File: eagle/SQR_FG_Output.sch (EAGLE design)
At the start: 17 parts, among them IC2 NJM7032, T1 2SK4017, T2 2SK4017

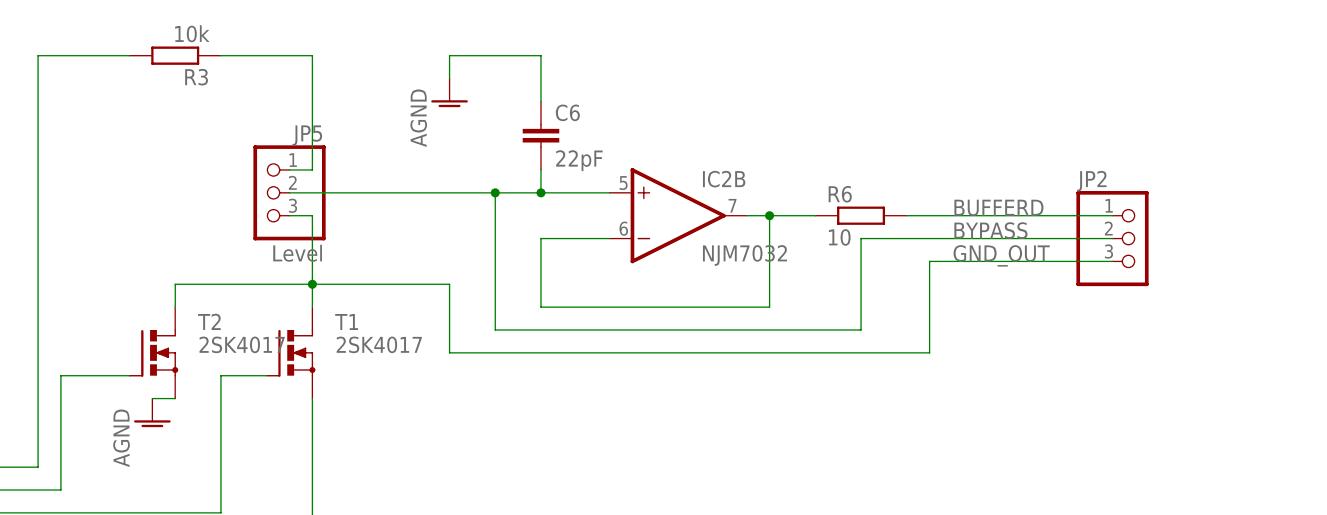
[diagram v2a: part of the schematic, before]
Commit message: SQR_FG_Output.sch LC 2次LPFを追加
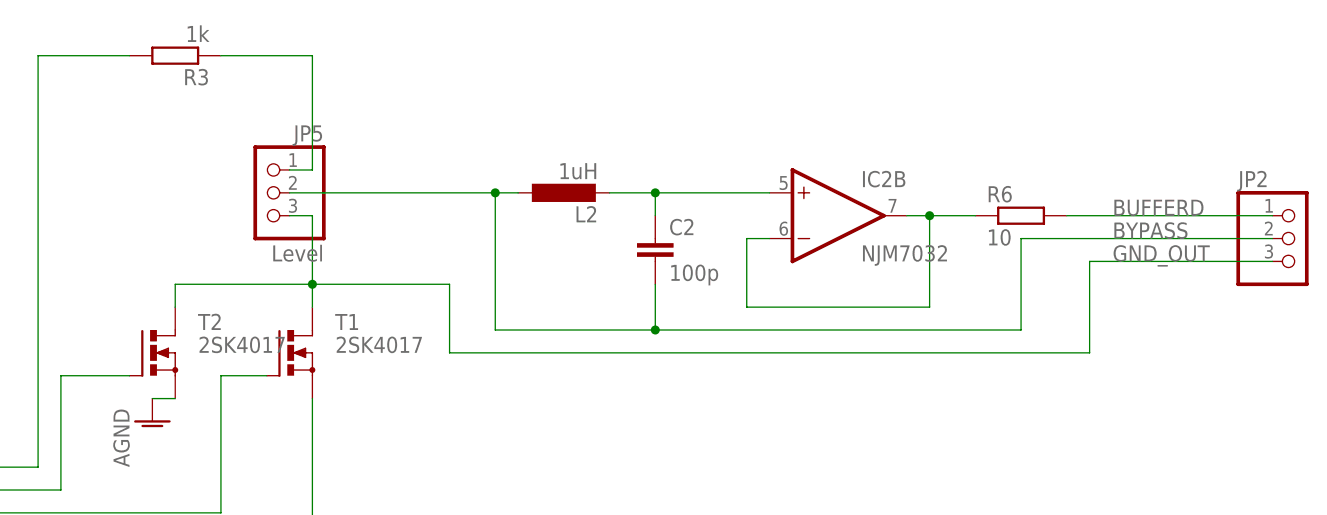
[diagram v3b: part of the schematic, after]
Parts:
- removed C6: 22pF, rcl:C-EU025-024X044
- added C2: 100p, rcl:C-EU050-024X044
- added L2: 1uH, rcl:L-EU0204/7
- R3: value 10k -> 1k
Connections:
- new net N$1: C2.1, IC2B.+IN, L2.2
- net AGND: no longer C6.1
- net BYPASS: now also C2.2, L2.1; no longer C6.2, IC2B.+IN
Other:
- moved on the sheet: IC2B, JP2, R6
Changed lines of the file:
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@@
 <setting verticaltext="up"/>
 </settings>
-<grid distance="0.1" unitdist="inch" unit="inch" style="dots" multiple="1" display="yes" altdistance="0.01" altunitdist="inch" altunit="inch"/>
+<grid distance="0.1" unitdist="inch" unit="inch" style="lines" multiple="1" display="no" altdistance="0.01" altunitdist="inch" altunit="inch"/>
 <layers>
 <layer number="1" name="Top" color="4" fill="1" visible="no" active="no"/>
@@
 <part name="T2" library="transistor-power" deviceset="RD06HVF1" device="" value="2SK4017"/>
 <part name="C5" library="rcl" deviceset="C-EU" device="025-024X044" value="0.1uF"/>
-<part name="R3" library="rcl" deviceset="R-EU_" device="0207/7" value="10k"/>
-<part name="C6" library="rcl" deviceset="C-EU" device="025-024X044" value="22pF"/>
+<part name="R3" library="rcl" deviceset="R-EU_" device="0207/7" value="1k"/>
 <part name="AGND1" library="supply1" deviceset="AGND" device=""/>
-<part name="AGND2" library="supply1" deviceset="AGND" device=""/>
 <part name="AGND3" library="supply1" deviceset="AGND" device=""/>
 <part name="AGND5" library="supply1" deviceset="AGND" device=""/>
@@
 <part name="AGND4" library="supply1" deviceset="AGND" device=""/>
 <part name="JP2" library="pinhead" deviceset="PINHD-1X3" device=""/>
+<part name="L2" library="rcl" deviceset="L-EU" device="0204/7" value="1uH"/>
+<part name="C2" library="rcl" deviceset="C-EU" device="050-024X044" value="100p"/>
 </parts>
 <sheets>
@@
 <instance part="P+3" gate="1" x="10.16" y="7.62"/>
 <instance part="IC2" gate="A" x="10.16" y="-7.62"/>
-<instance part="IC2" gate="B" x="71.12" y="58.42"/>
+<instance part="IC2" gate="B" x="88.9" y="58.42"/>
 <instance part="IC2" gate="P" x="10.16" y="-7.62"/>
-<instance part="R6" gate="G$1" x="91.44" y="58.42"/>
+<instance part="R6" gate="G$1" x="109.22" y="58.42"/>
 <instance part="R7" gate="G$1" x="-20.32" y="2.54" rot="R90"/>
 <instance part="R8" gate="G$1" x="-20.32" y="-12.7" rot="R90"/>
@@
 <instance part="C5" gate="G$1" x="15.24" y="2.54" rot="R90"/>
 <instance part="R3" gate="G$1" x="15.24" y="76.2" rot="R180"/>
-<instance part="C6" gate="G$1" x="55.88" y="68.58"/>
 <instance part="AGND1" gate="VR1" x="12.7" y="35.56"/>
-<instance part="AGND2" gate="VR1" x="45.72" y="71.12"/>
 <instance part="AGND3" gate="VR1" x="10.16" y="-22.86"/>
 <instance part="AGND5" gate="VR1" x="-20.32" y="-22.86"/>
@@
 <instance part="L1" gate="G$1" x="-12.7" y="50.8"/>
 <instance part="AGND4" gate="VR1" x="-12.7" y="40.64"/>
-<instance part="JP2" gate="A" x="121.92" y="55.88"/>
+<instance part="JP2" gate="A" x="139.7" y="55.88"/>
+<instance part="L2" gate="G$1" x="58.42" y="60.96" rot="R90"/>
+<instance part="C2" gate="G$1" x="68.58" y="55.88"/>
 </instances>
 <busses>
@@
 <net name="N$16" class="0">
 <segment>
-<wire x1="55.88" y1="55.88" x2="55.88" y2="48.26" width="0.1524" layer="91"/>
+<wire x1="78.74" y1="55.88" x2="78.74" y2="48.26" width="0.1524" layer="91"/>
 <pinref part="IC2" gate="B" pin="-IN"/>
-<wire x1="55.88" y1="55.88" x2="63.5" y2="55.88" width="0.1524" layer="91"/>
+<wire x1="78.74" y1="55.88" x2="81.28" y2="55.88" width="0.1524" layer="91"/>
 <pinref part="R6" gate="G$1" pin="1"/>
 <pinref part="IC2" gate="B" pin="OUT"/>
-<wire x1="78.74" y1="58.42" x2="81.28" y2="58.42" width="0.1524" layer="91"/>
-<wire x1="81.28" y1="58.42" x2="86.36" y2="58.42" width="0.1524" layer="91"/>
-<wire x1="55.88" y1="48.26" x2="81.28" y2="48.26" width="0.1524" layer="91"/>
-<wire x1="81.28" y1="48.26" x2="81.28" y2="58.42" width="0.1524" layer="91"/>
-<junction x="81.28" y="58.42"/>
+<wire x1="96.52" y1="58.42" x2="99.06" y2="58.42" width="0.1524" layer="91"/>
+<wire x1="99.06" y1="58.42" x2="104.14" y2="58.42" width="0.1524" layer="91"/>
+<wire x1="78.74" y1="48.26" x2="99.06" y2="48.26" width="0.1524" layer="91"/>
+<wire x1="99.06" y1="48.26" x2="99.06" y2="58.42" width="0.1524" layer="91"/>
+<junction x="99.06" y="58.42"/>
 </segment>
 </net>
@@
 <segment>
 <pinref part="R6" gate="G$1" pin="2"/>
-<wire x1="96.52" y1="58.42" x2="119.38" y2="58.42" width="0.1524" layer="91"/>
+<wire x1="114.3" y1="58.42" x2="137.16" y2="58.42" width="0.1524" layer="91"/>
 <pinref part="JP2" gate="A" pin="1"/>
-<label x="101.6" y="58.42" size="1.778" layer="95"/>
+<label x="119.38" y="58.42" size="1.778" layer="95"/>
 </segment>
 </net>
@@
 <wire x1="30.48" y1="50.8" x2="45.72" y2="50.8" width="0.1524" layer="91"/>
 <wire x1="45.72" y1="50.8" x2="45.72" y2="43.18" width="0.1524" layer="91"/>
-<wire x1="45.72" y1="43.18" x2="99.06" y2="43.18" width="0.1524" layer="91"/>
-<wire x1="99.06" y1="43.18" x2="99.06" y2="53.34" width="0.1524" layer="91"/>
+<wire x1="45.72" y1="43.18" x2="116.84" y2="43.18" width="0.1524" layer="91"/>
+<wire x1="116.84" y1="43.18" x2="116.84" y2="53.34" width="0.1524" layer="91"/>
 <pinref part="JP5" gate="A" pin="3"/>
 <wire x1="27.94" y1="58.42" x2="30.48" y2="58.42" width="0.1524" layer="91"/>
 <pinref part="JP2" gate="A" pin="3"/>
-<wire x1="119.38" y1="53.34" x2="99.06" y2="53.34" width="0.1524" layer="91"/>
-<label x="101.6" y="53.34" size="1.778" layer="95"/>
+<wire x1="137.16" y1="53.34" x2="116.84" y2="53.34" width="0.1524" layer="91"/>
+<label x="119.38" y="53.34" size="1.778" layer="95"/>
 </segment>
 </net>
@@
 <segment>
 <wire x1="27.94" y1="60.96" x2="50.8" y2="60.96" width="0.1524" layer="91"/>
-<pinref part="C6" gate="G$1" pin="2"/>
-<wire x1="50.8" y1="60.96" x2="55.88" y2="60.96" width="0.1524" layer="91"/>
-<wire x1="55.88" y1="63.5" x2="55.88" y2="60.96" width="0.1524" layer="91"/>
 <pinref part="JP5" gate="A" pin="2"/>
-<pinref part="IC2" gate="B" pin="+IN"/>
-<wire x1="63.5" y1="60.96" x2="55.88" y2="60.96" width="0.1524" layer="91"/>
-<junction x="55.88" y="60.96"/>
 <pinref part="JP2" gate="A" pin="2"/>
-<wire x1="119.38" y1="55.88" x2="91.44" y2="55.88" width="0.1524" layer="91"/>
-<wire x1="91.44" y1="55.88" x2="91.44" y2="45.72" width="0.1524" layer="91"/>
-<wire x1="91.44" y1="45.72" x2="50.8" y2="45.72" width="0.1524" layer="91"/>
+<wire x1="137.16" y1="55.88" x2="109.22" y2="55.88" width="0.1524" layer="91"/>
+<wire x1="109.22" y1="55.88" x2="109.22" y2="45.72" width="0.1524" layer="91"/>
+<wire x1="109.22" y1="45.72" x2="68.58" y2="45.72" width="0.1524" layer="91"/>
+<wire x1="68.58" y1="45.72" x2="50.8" y2="45.72" width="0.1524" layer="91"/>
 <wire x1="50.8" y1="45.72" x2="50.8" y2="60.96" width="0.1524" layer="91"/>
+<label x="119.38" y="55.88" size="1.778" layer="95"/>
+<pinref part="L2" gate="G$1" pin="1"/>
+<wire x1="50.8" y1="60.96" x2="53.34" y2="60.96" width="0.1524" layer="91"/>
 <junction x="50.8" y="60.96"/>
-<label x="101.6" y="55.88" size="1.778" layer="95"/>
+<pinref part="C2" gate="G$1" pin="2"/>
+<wire x1="68.58" y1="50.8" x2="68.58" y2="45.72" width="0.1524" layer="91"/>
+<junction x="68.58" y="45.72"/>
 </segment>
 </net>
@@
 <pinref part="AGND1" gate="VR1" pin="AGND"/>
 <wire x1="12.7" y1="38.1" x2="15.24" y2="38.1" width="0.1524" layer="91"/>
-</segment>
-<segment>
-<pinref part="C6" gate="G$1" pin="1"/>
-<wire x1="55.88" y1="71.12" x2="55.88" y2="76.2" width="0.1524" layer="91"/>
-<wire x1="55.88" y1="76.2" x2="45.72" y2="76.2" width="0.1524" layer="91"/>
-<wire x1="45.72" y1="76.2" x2="45.72" y2="73.66" width="0.1524" layer="91"/>
-<pinref part="AGND2" gate="VR1" pin="AGND"/>
 </segment>
 <segment>
@@
 </segment>
 </net>
+<net name="N$1" class="0">
+<segment>
+<pinref part="L2" gate="G$1" pin="2"/>
+<pinref part="IC2" gate="B" pin="+IN"/>
+<wire x1="63.5" y1="60.96" x2="68.58" y2="60.96" width="0.1524" layer="91"/>
+<pinref part="C2" gate="G$1" pin="1"/>
+<wire x1="68.58" y1="60.96" x2="81.28" y2="60.96" width="0.1524" layer="91"/>
+<wire x1="68.58" y1="58.42" x2="68.58" y2="60.96" width="0.1524" layer="91"/>
+<junction x="68.58" y="60.96"/>
+</segment>
+</net>

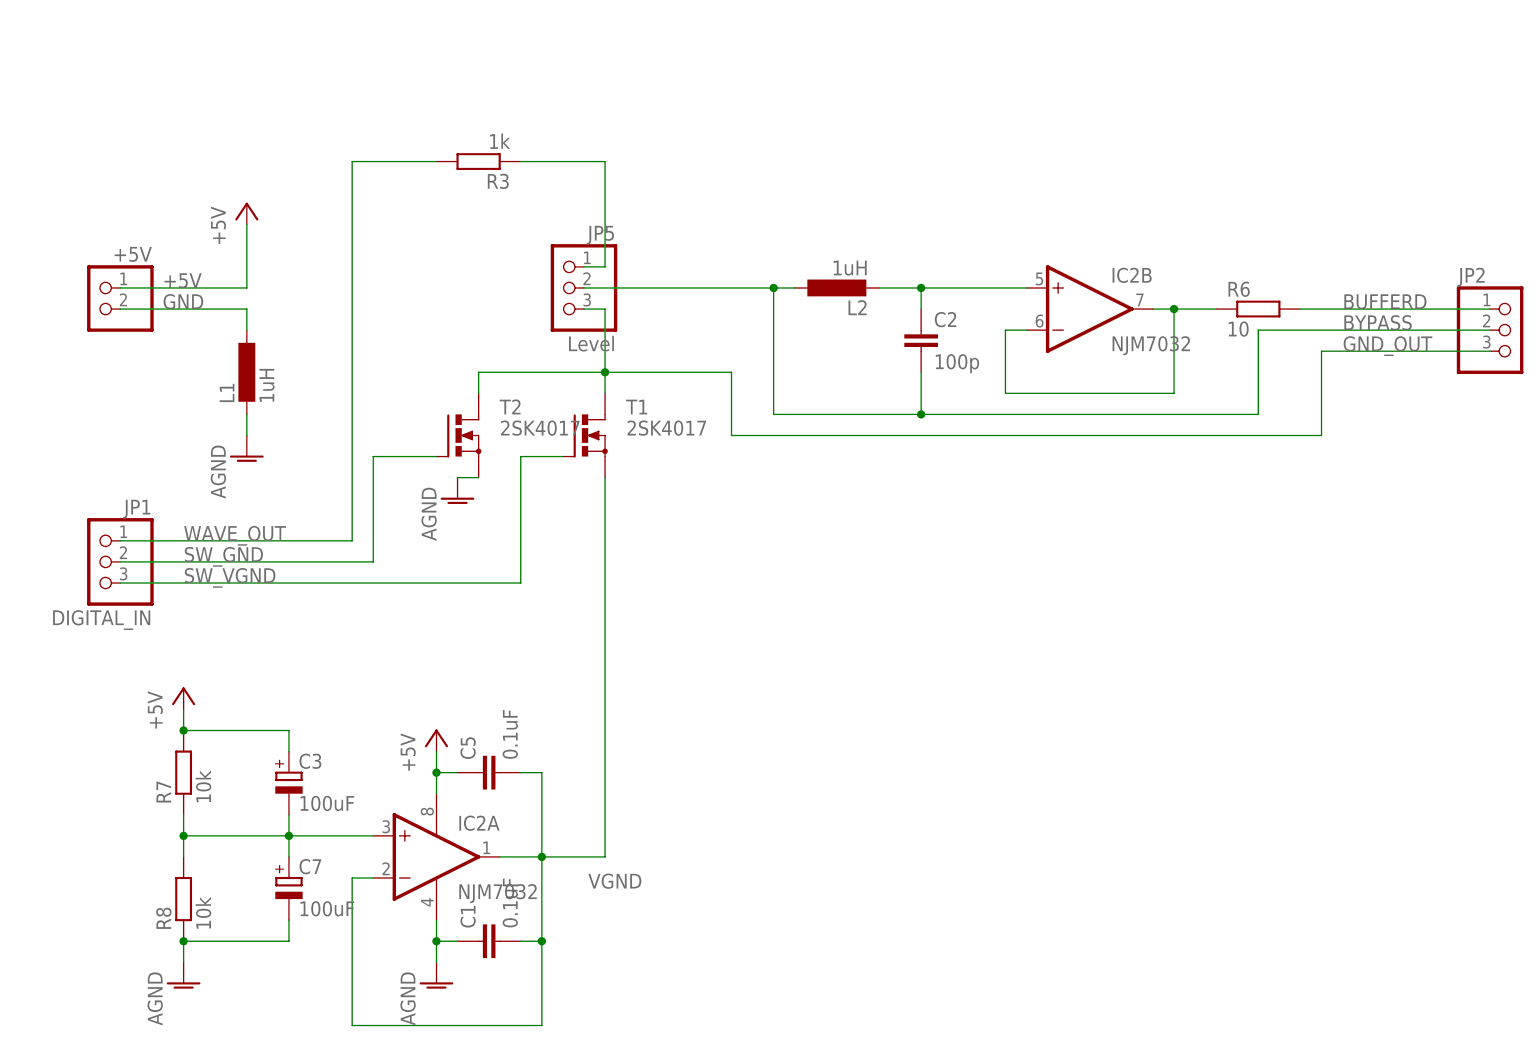
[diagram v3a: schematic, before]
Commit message: SQR_FG_Output.sch, brd: MOS-FETのGate, Drain, Sourceの並びを修正
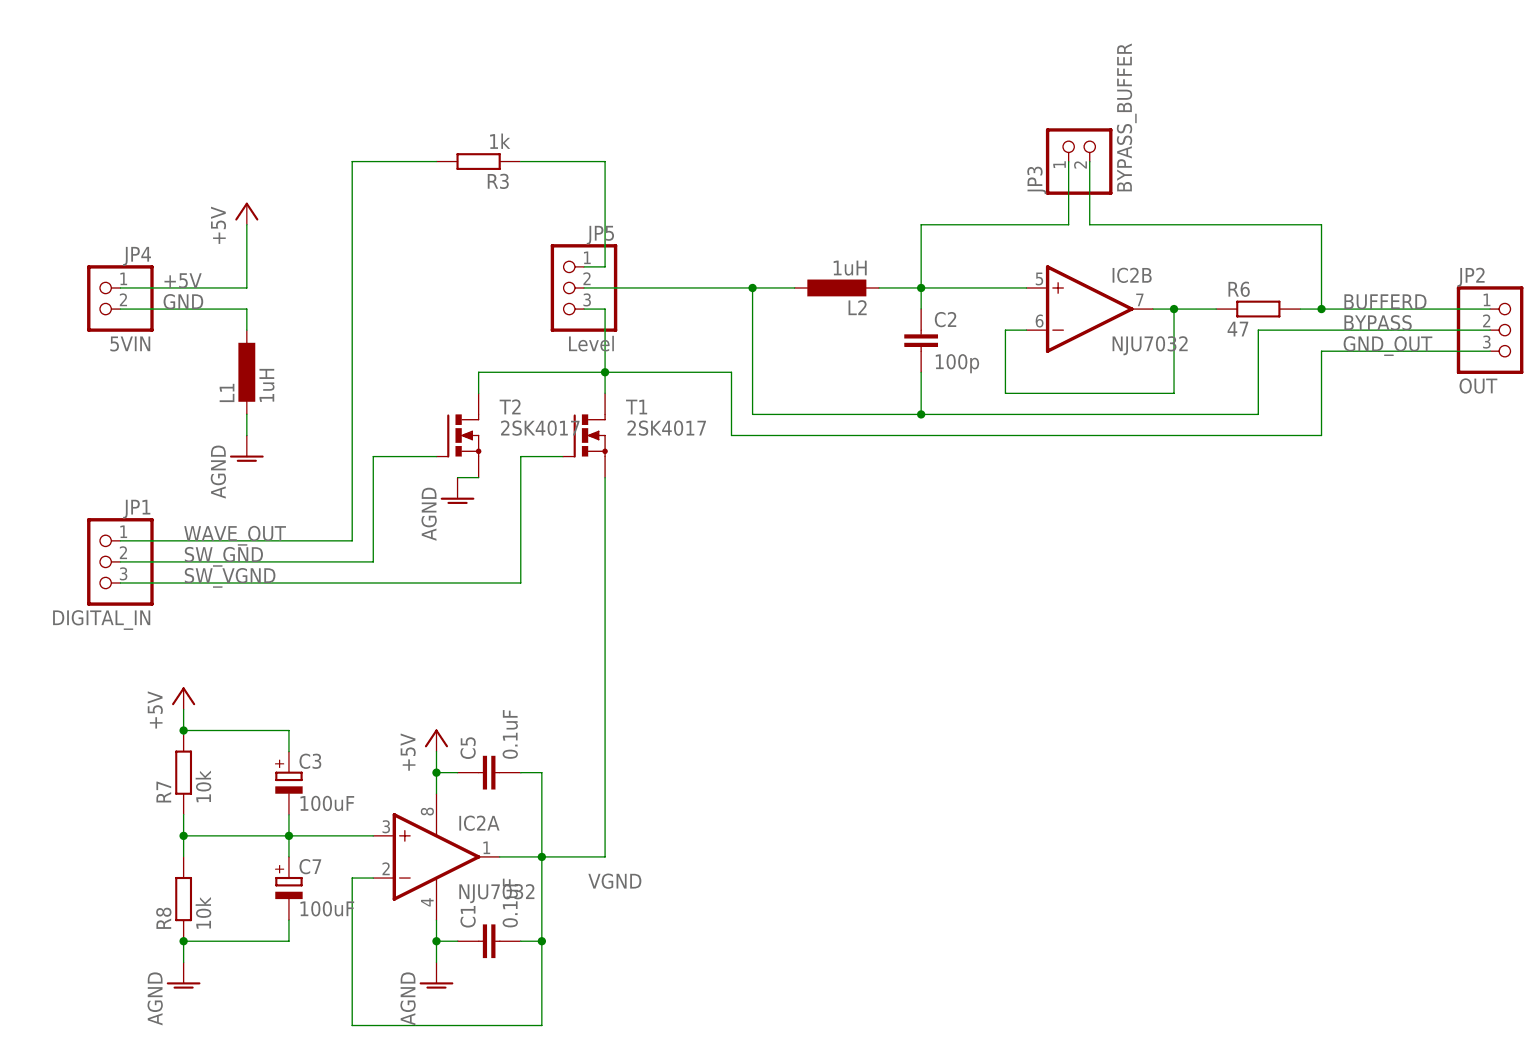
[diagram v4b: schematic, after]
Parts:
- added JP3: BYPASS_BUFFER, pinhead:PINHD-1X2
- C2: device rcl:C-EU050-024X044 -> rcl:C-EU075-032X103
- IC2: value NJM7032 -> NJU7032
- JP2: value (none) -> OUT
- JP4: value (none) -> 5VIN
- R6: value 10 -> 47
- T1, T2: device transistor-power:RD06HVF1 -> transistor-power:BUZ11BV
- renumbered +5V to JP4
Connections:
- net BUFFERD: now also JP3.2
- net N$1: now also JP3.1
